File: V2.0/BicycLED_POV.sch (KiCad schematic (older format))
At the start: 57 parts, among them IC1 AT45DBXX1, IC2 AT91SAM7S512/256/128/64/321-AU, P1 CONN_2, Q1 BSH207, Q2 BSH207, Q3 2N2002K, SW1 bootloader, U1 CONN_MICROSD, U2 MCP73811/2, U3 CONN_JTAG_ARM, U4 USBCONN, U5 AH173, U6 FAN2502-XX, X1 18.432 MHz

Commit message: sch: Added ADC Voltage Regulator
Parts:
- added C28: 100nF, symbol C
- added R79, R80, R81, R82, R83: R, symbol R
- added U15: TS3431, symbol TS3431
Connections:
- net labels added: Bat_monit, Vref
- wire segments 197 -> 212
- no-connect marks 33 -> 31
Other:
- note added: "ADC Voltage Reference"
- note added: "I max = 1mA"
- note added: "Internal Pull-UP\n(10K)"
- note removed: "Internal Pull-UP (10K)"
- moved on the sheet: C1, C10, C11, C12, C13, C14, C15, C16, C17, C18, C19, C20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

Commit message: 
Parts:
- removed R82, R83: R, symbol R
- removed U15: TS3431, symbol TS3431
- added C29: 100nF, symbol C
- R81: value R -> 1K
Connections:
- net labels removed: Vref
- wire segments 212 -> 282
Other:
- note removed: "ADC Voltage Reference"
- note removed: "I max = 1mA"

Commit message: Symbols and Modules modifications.
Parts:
- removed BT1: Rechar. Lithium batt 3.7V 900mAh, symbol BATTERY
- removed Q1, Q2: BSH207, SOT457, symbol BSH207-SOT457
- removed U1: CONN_MICROSD, symbol CONN_microSD
- removed U4: USBCONN, symbol USBCONN
- added BT1: BATTERY_HOLDER, symbol BATTERY_HOLDER
- added J1: CONN_USB, symbol CONN_USB
- added J2: CONN_MICRO_SD, symbol CONN_MICRO_SD
- added Q1, Q2: NTR417P, SM0805, symbol NTR417P
- C10, C5, C7, P1, R1, R2, R3, R8: footprint (none) -> SM0805
- C12: renamed from C11; footprint (none) -> SM0805
- C13: renamed from C12; footprint (none) -> SM0805
- C14: renamed from C13; footprint (none) -> SM0805
- C15: renamed from C14; footprint (none) -> SM0805
- C16: renamed from C15; footprint (none) -> SM0805
- C18: renamed from C17; footprint (none) -> SM0805
- C19: renamed from C18; footprint (none) -> SM0805
- C20: renamed from C19; footprint (none) -> SM0805
- C21: renamed from C20; footprint (none) -> SM0805
- C22: renamed from C21; footprint (none) -> SM0805
- C24: renamed from C23; footprint (none) -> SM0805
- C25: renamed from C24; footprint (none) -> SM0805
- C26: renamed from C25; footprint (none) -> SM0805
- C27: renamed from C26; footprint (none) -> SM0805
- C4: renamed from C28; footprint (none) -> SM0805
- C8: renamed from C6; footprint (none) -> SM0805
- C9: renamed from C8; footprint (none) -> SM0805
- Q3: footprint SOT23 -> SM0805
- R4: renamed from R5; footprint (none) -> SM0805
- R9: renamed from R79; footprint (none) -> SM0805
- renumbered C2 to C1, C9 to C11, C16 to C17, C4 to C2, C22 to C23, C29 to C28, C27 to C29, C1 to C6, R80 to R10, R9 to R11, R10 to R12, R11 to R13, R12 to R14, R13 to R15, R14 to R16, R81 to R17, R4 to R5, U3 to U1, U2 to U3, U5 to U4, U6 to U5
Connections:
- wire segments 282 -> 203
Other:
- note removed: "uSD Card"
- moved on the sheet: C5

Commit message: 
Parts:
- added C30: C, symbol C
- added R82, R83: R, symbol R
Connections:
- wire segments 203 -> 209
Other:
- note added: "PCB: Can be\nmounted SMD\nor TH version."
- note removed: "Internal Pull-UP\n(10K)"
- note removed: "PCB: Can be mounted SMD or TH version."
- moved on the sheet: U4

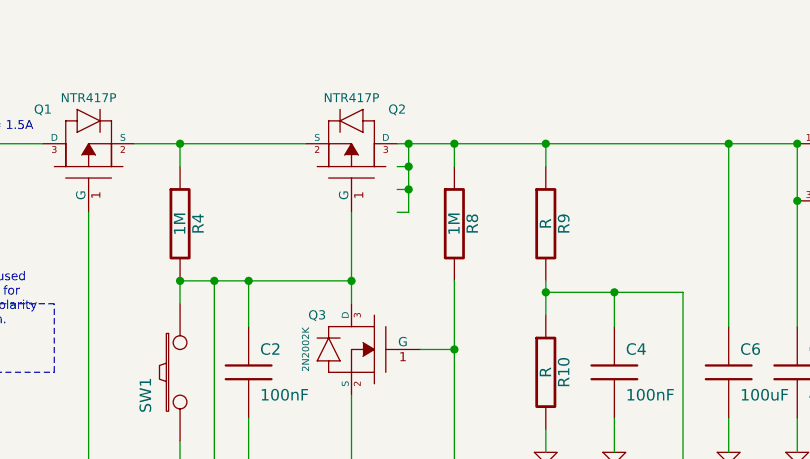
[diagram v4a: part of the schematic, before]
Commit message: 
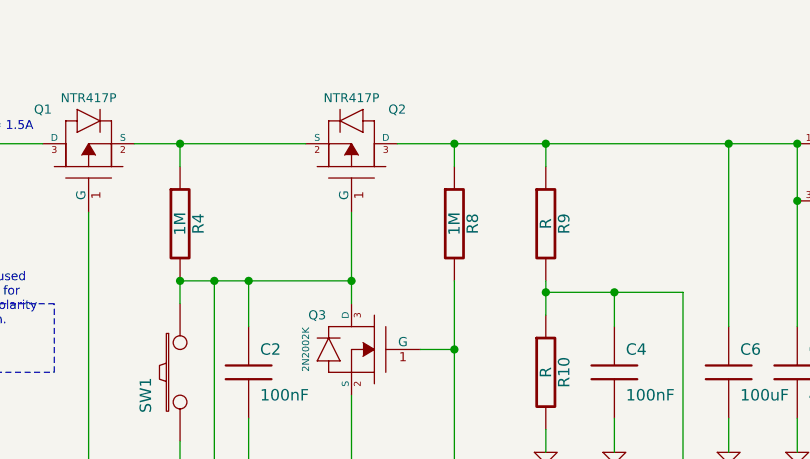
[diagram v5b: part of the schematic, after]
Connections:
- wire segments 209 -> 205
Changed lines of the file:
@@
-EESchema Schematic File Version 2  date 25/05/2010 20:48:09
+EESchema Schematic File Version 2  date 28/05/2010 02:56:11
 LIBS:regul
 LIBS:switch_FSM2JSMA
@@
 Sheet 1 2
 Title "   BicycLED POV"
-Date "25 may 2010"
+Date "28 may 2010"
 Rev "v 2.0"
 Comp "Hardware BOX                                http://code.google.com/p/bicycleledpov"
@@
 	3200 1350 3200 1750
 Connection ~ 3200 1650
-Connection ~ 3450 1050
-Connection ~ 3450 1150
-Wire Wire Line
-	3400 1150 3450 1150
-Wire Wire Line
-	3450 1050 3450 1350
-Wire Wire Line
-	3450 1350 3400 1350
-Wire Wire Line
-	3400 1250 3450 1250
-Connection ~ 3450 1250
 Wire Wire Line
 	2450 2350 2450 2450
